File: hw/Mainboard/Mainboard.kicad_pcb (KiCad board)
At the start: 2 copper layers, 262.5 x 95.2 mm, 272 parts, among them J1 SJ-43504-SMT-TR, J10 5V PWR, J11 9V POWER, J12 NOT_HDMI_A, J13 MicroSD, J14 USB2.0_HOST_TYPE_C, J16 MCU, J17 BOOTSEL, J18 PET POWER, J19 PROG, J2 KEYBOARD, J20 5V PWR, J21 FPGA-P4, J22 MENU, J23 FPGA_P2, J24 Conn_02x15_Odd_Even, J3 IEEE, J4 USER, J5 CASS A, J6 CASS B, J7 9V POWER, J8 SPEAKER, J9 VIDEO, Q1 AO3401A, Q2 MMBT3904, Q3 AO3401A, Q4 MMBT3904, SW1 RESET, SW2 RUN, SW3 MENU, SW4 NMI, SW5 CONFIG, U1 74HC154, U10 LM317AG-TN3-R, U11 W65C02S, U12 AS6C1008, U13 AMS1117-3.3, U14 RP2040, U15 LM317AG-TN3-R, U16 W25Q128JVS, U17 LM317AG-TN3-R, U18 SN74LVC4245APWR, U19 SN74LVC4245APWR, U2 SN74LS07, U20 SN74LVC4245APWR, U21 T8Q144C3, U3 SN74LS07, U4 SN74LS07, U5 74LS245, U6 74LS245, U7 W65C21N, U8 W65C21N, U9 W65C22N, Y1 12 MHz

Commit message: wip: support 8x16 keyboard matrix
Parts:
- added C53: 100n, Capacitor_SMD:C_0402_1005Metric, F.Cu at (-113.5, 72.2)
- added J15: KEYBOARDEX, Connector_PinHeader_2.54mm:PinHeader_1x09_P2.54mm_Vertical, F.Cu at (-92.9, 81.3)
- added Q5: SS8550, Package_TO_SOT_SMD:SOT-23, F.Cu at (-100.4, 72.8)
- added R48: 33, Resistor_SMD:R_0402_1005Metric, F.Cu at (-19.7, 56.3)
- added R51: 33, Resistor_SMD:R_0402_1005Metric, F.Cu at (-20.9, 54.3)
- added R63: 33, Resistor_SMD:R_0402_1005Metric, F.Cu at (-15.9, 54.3)
- added R67: 33, Resistor_SMD:R_0402_1005Metric, F.Cu at (-17.1, 54.3)
- added R68: 33, Resistor_SMD:R_0402_1005Metric, F.Cu at (-54.0, 42.2)
- added R69: 33, Resistor_SMD:R_0402_1005Metric, F.Cu at (-4.26, 62.1)
- added R70: 33, Resistor_SMD:R_0402_1005Metric, F.Cu at (-52.0, 32.5)
- added R71: 33, Resistor_SMD:R_0402_1005Metric, F.Cu at (-52.0, 38.1)
- added R72: 2k2, Resistor_SMD:R_0402_1005Metric, F.Cu at (-101.5, 75.0)
- added R73: 2k2, Resistor_SMD:R_0402_1005Metric, F.Cu at (-101.4, 70.5)
- added R74: 2k2, Resistor_SMD:R_0402_1005Metric, F.Cu at (-99.5, 75.0)
- added U22: 74LS145, Package_SO:SOIC-16_3.9x9.9mm_P1.27mm, F.Cu at (-107.7, 74.8)
- J16: footprint Connector_PinHeader_2.54mm:PinHeader_2x10_P2.54mm_Vertical -> Connector_PinHeader_2.54mm:PinHeader_2x12_P2.54mm_Vertical
- U1: value 74HC154 -> 74LS145; footprint Package_SO:TSSOP-24_4.4x7.8mm_P0.65mm -> Package_SO:SOIC-16_3.9x9.9mm_P1.27mm
- moved R66 48.7 mm to (-18.5, 22.3)
- moved C1 9.87 mm to (-126.3, 72.3), turned to -90 degrees
- moved U1 8.93 mm to (-120.5, 74.8)
- moved R21 4.00 mm to (-21.9, 60.6)
- moved R65 3.61 mm to (-37.6, 26.7)
- moved RN10 2.78 mm to (-130.0, 79.2)
- moved J16 2.55 mm to (-47.1, 22.3)
- moved R52 2.54 mm to (-71.2, 7.70)
- moved R54 2.54 mm to (-73.2, 7.70)
- moved R55 2.54 mm to (-71.2, 5.30)
- moved R57 2.54 mm to (-71.2, 6.35)
- moved R58 2.54 mm to (-73.2, 6.35)
- moved R60 2.54 mm to (-73.2, 5.30)
- moved R64 2.31 mm to (-38.6, 25.6)
- moved U20 2.18 mm to (-93.0, 61.3)
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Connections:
- C1 pad 1: Net-(C1-Pad1) -> /Keyboard/VCC
- C1 pad 2: Net-(C1-Pad2) -> /Keyboard/VSS
- J13 pad 3: /MAGIC/MCU/SPI1_TX -> /MAGIC/FPGA/SPI0_TX
- J13 pad 5: /MAGIC/MCU/SPI1_SCK -> /MAGIC/FPGA/SPI0_SCK
- J13 pad 7: /MAGIC/MCU/SPI1_RX -> Net-(J13-Pad7)
- J16 pad 10: /MAGIC/MCU/SPI1_~{READY} -> /MAGIC/FPGA/YY1
- J16 pad 11: /MAGIC/MCU/SPI0_SCK -> /MAGIC/FPGA/YY2
- J16 pad 12: /MAGIC/MCU/SPI1_RX -> /MAGIC/FPGA/YY3
- J16 pad 13: /MAGIC/MCU/SPI0_TX -> /MAGIC/FPGA/YY4
- J16 pad 14: /MAGIC/MCU/SPI1_~{CS} -> /MAGIC/FPGA/SPI1_~{READY}
- J16 pad 15: /MAGIC/MCU/SPI0_RX -> /MAGIC/FPGA/YY5
- J16 pad 16: /MAGIC/MCU/SPI1_SCK -> /MAGIC/FPGA/SPI1_~{CS}
- J16 pad 17: unconnected-(J16-Pad17) -> /MAGIC/MCU/I2C0_SDA
- J16 pad 18: /MAGIC/MCU/SPI1_TX -> /MAGIC/FPGA/SPI1_SCK
- J16 pad 19: unconnected-(J16-Pad19) -> /MAGIC/MCU/I2C0_SCL
- J16 pad 2: +3V3 -> +1V1
- J16 pad 20: GND -> /MAGIC/FPGA/SPI1_TX
- J16 pad 3: /MAGIC/MCU/I2C0_SDA -> /MAGIC/FPGA/SPI0_~{CS}
- J16 pad 4: /MAGIC/MCU/I2C1_SDA -> /MAGIC/FPGA/I2C1_SDA
- J16 pad 5: /MAGIC/MCU/I2C0_SCL -> /MAGIC/FPGA/SPI0_SCK
- J16 pad 6: /MAGIC/MCU/I2C1_SCL -> /MAGIC/FPGA/I2C1_SCL
- J16 pad 7: GND -> /MAGIC/FPGA/SPI0_TX
- J16 pad 8: /MAGIC/MCU/CEC -> /MAGIC/FPGA/YY6
- J16 pad 9: /MAGIC/MCU/SPI0_~{CS} -> /MAGIC/FPGA/SPI0_RX
- J19 pad 12: /MAGIC/MCU/SPI0_~{CS} -> /MAGIC/FPGA/SPI0_~{CS}
- J21 pad 11: /MAGIC/FPGA/R76 -> /MAGIC/FPGA/L75
- J21 pad 12: GND -> /MAGIC/FPGA/R76
- J21 pad 15: /MAGIC/FPGA/FPGA_CLK -> /MAGIC/FPGA/S1
- J21 pad 16: unconnected-(J21-Pad16) -> /MAGIC/FPGA/FPGA_CLK
- J21 pad 17: /MAGIC/FPGA/S2 -> /MAGIC/FPGA/NSTATUS
- J21 pad 18: /MAGIC/FPGA/S1 -> /MAGIC/FPGA/S2
- J21 pad 19: /MAGIC/FPGA/S3 -> /MAGIC/FPGA/S4
- J21 pad 20: /MAGIC/FPGA/NSTATUS -> /MAGIC/FPGA/S3
- J21 pad 21: /MAGIC/FPGA/L68 -> /MAGIC/FPGA/L67
- J21 pad 22: /MAGIC/FPGA/S4 -> /CPU \ RAM/~{NMI}
- J21 pad 23: /MAGIC/FPGA/L65 -> /MAGIC/FPGA/L66
- J21 pad 24: /MAGIC/FPGA/L67 -> /MAGIC/FPGA/L65
- J21 pad 25: /MAGIC/FPGA/L64 -> /MAGIC/FPGA/L53
- J21 pad 26: /MAGIC/FPGA/L66 -> /MAGIC/FPGA/L64
- J23 pad 10: /MAGIC/FPGA/N02 -> /MAGIC/FPGA/N04
- J23 pad 11: unconnected-(J23-Pad11) -> /MAGIC/FPGA/P06
- J23 pad 12: unconnected-(J23-Pad12) -> /MAGIC/FPGA/N06
- J23 pad 13: /MAGIC/FPGA/DIAG -> /MAGIC/FPGA/P09
- J23 pad 14: /MAGIC/FPGA/VIA_CB2 -> /MAGIC/FPGA/N09
- J23 pad 15: /MAGIC/FPGA/GRAPHICS -> /MAGIC/FPGA/DIAG
- J23 pad 16: /MAGIC/FPGA/~{RAM_OE} -> /MAGIC/FPGA/VIA_CB2
- J23 pad 17: /MAGIC/FPGA/~{RAM_WE} -> /MAGIC/FPGA/GRAPHICS
- J23 pad 18: /MAGIC/FPGA/~{VP} -> /MAGIC/FPGA/~{RAM_OE}
- J23 pad 19: /MAGIC/FPGA/RDY -> /MAGIC/FPGA/~{RAM_WE}
- J23 pad 20: /CPU \ RAM/~{RES} -> /MAGIC/FPGA/~{VP}
- J23 pad 21: /MAGIC/FPGA/~{SO} -> /MAGIC/FPGA/RDY
- J23 pad 22: /MAGIC/FPGA/~{IRQ} -> /MAGIC/FPGA/~{SO}
- J23 pad 23: /MAGIC/FPGA/~{ML} -> /MAGIC/FPGA/~{IRQ}
- J23 pad 24: /MAGIC/FPGA/BE -> /MAGIC/FPGA/~{ML}
- J23 pad 25: /CPU \ RAM/~{NMI} -> /MAGIC/FPGA/BE
- J23 pad 27: GND -> /CPU \ RAM/~{RES}
- J23 pad 3: GND -> unconnected-(J23-Pad3)
- J23 pad 4: /MAGIC/FPGA/AUDIO -> unconnected-(J23-Pad4)
- J23 pad 5: unconnected-(J23-Pad5) -> /MAGIC/FPGA/AUDIO
- J23 pad 7: unconnected-(J23-Pad7) -> /MAGIC/FPGA/P02
- J23 pad 8: /MAGIC/FPGA/P02 -> /MAGIC/FPGA/N02
- J23 pad 9: unconnected-(J23-Pad9) -> /MAGIC/FPGA/P04
- JP7 pad 1: /MAGIC/MCU/CEC -> /MAGIC/FPGA/CEC
- PT17 pad 2: Net-(C1-Pad1) -> /Keyboard/VCC
- PT33 pad 2: Net-(C1-Pad2) -> /Keyboard/VSS
- R19 pad 1: /MAGIC/MCU/SPI0_SCK -> /MAGIC/FPGA/SPI0_SCK
- R22 pad 1: /MAGIC/MCU/SPI1_SCK -> /MAGIC/FPGA/SPI1_SCK
- R64 pad 2: /MAGIC/MCU/I2C1_SDA -> /MAGIC/FPGA/I2C1_SDA
- R65 pad 2: /MAGIC/MCU/I2C1_SCL -> /MAGIC/FPGA/I2C1_SCL
- RN10 pad 5: Net-(C1-Pad1) -> /Keyboard/VCC
- RN10 pad 6: Net-(C1-Pad1) -> /Keyboard/VCC
- RN10 pad 7: Net-(C1-Pad1) -> /Keyboard/VCC
- RN10 pad 8: Net-(C1-Pad1) -> /Keyboard/VCC
- RN16 pad 3: /MAGIC/MCU/SPI1_TX -> /MAGIC/FPGA/SPI0_TX
- RN16 pad 4: /MAGIC/MCU/SPI1_RX -> /MAGIC/FPGA/SPI0_RX
- RN9 pad 5: Net-(C1-Pad1) -> /Keyboard/VCC
- RN9 pad 6: Net-(C1-Pad1) -> /Keyboard/VCC
- RN9 pad 7: Net-(C1-Pad1) -> /Keyboard/VCC
- RN9 pad 8: Net-(C1-Pad1) -> /Keyboard/VCC
- U1 pad 10: /Keyboard/R9 -> /Keyboard/R8
- U1 pad 11: unconnected-(U1-Pad11) -> /Keyboard/R9
- U1 pad 12: Net-(C1-Pad2) -> /IO/KEY_ROW3
- U1 pad 13: unconnected-(U1-Pad13) -> /IO/KEY_ROW2
- U1 pad 14: unconnected-(U1-Pad14) -> /IO/KEY_ROW1
- U1 pad 15: unconnected-(U1-Pad15) -> /IO/KEY_ROW0
- U1 pad 16: unconnected-(U1-Pad16) -> /Keyboard/VCC
- U1 pad 8: /Keyboard/R7 -> /Keyboard/VSS
- U1 pad 9: /Keyboard/R8 -> /Keyboard/R7
- U14 pad 13: /MAGIC/MCU/SPI1_~{READY} -> /MAGIC/FPGA/SPI1_~{READY}
- U14 pad 14: /MAGIC/MCU/MCU_FPGA_CLK -> /MAGIC/MCU/MCU_SPI1_TX
- U14 pad 15: /MAGIC/MCU/SPI1_RX -> /MAGIC/FPGA/SPI1_RX
- U14 pad 16: /MAGIC/MCU/SPI1_~{CS} -> /MAGIC/MCU/MCU_SPI1_~{CS}
- U14 pad 18: /MAGIC/MCU/SPI1_TX -> /MAGIC/MCU/MCU_FPGA_CLK
- U14 pad 36: /MAGIC/MCU/CEC -> /MAGIC/FPGA/CEC
- U14 pad 4: /MAGIC/MCU/I2C1_SDA -> /MAGIC/FPGA/I2C1_SDA
- U14 pad 5: /MAGIC/MCU/I2C1_SCL -> /MAGIC/FPGA/I2C1_SCL
- U14 pad 6: /MAGIC/MCU/SPI0_RX -> /MAGIC/FPGA/SPI0_RX
- U14 pad 7: /MAGIC/MCU/SPI0_~{CS} -> /MAGIC/MCU/MCU_SPI0_~{CS}
- U14 pad 9: /MAGIC/MCU/SPI0_TX -> /MAGIC/MCU/MCU_SPI0_TX
- U21 pad 10: /MAGIC/MCU/SPI1_~{CS} -> /MAGIC/FPGA/SPI1_~{CS}
- U21 pad 11: /MAGIC/MCU/SPI1_SCK -> /MAGIC/FPGA/SPI1_SCK
- U21 pad 119: /MAGIC/~{PIA2_CS} -> /MAGIC/~{IO_OE}
- U21 pad 123: /MAGIC/~{IO_OE} -> /MAGIC/~{PIA2_CS}
- U21 pad 131: unconnected-(U21-Pad131) -> /MAGIC/FPGA/L75
- U21 pad 139: /MAGIC/FPGA/L68 -> /CPU \ RAM/~{NMI}
- U21 pad 14: /MAGIC/MCU/I2C1_SCL -> /MAGIC/FPGA/FPGA_SPI1_~{READY}
- U21 pad 15: /MAGIC/MCU/I2C1_SDA -> /MAGIC/FPGA/I2C1_SCL
- U21 pad 16: unconnected-(U21-Pad16) -> /MAGIC/FPGA/I2C1_SDA
- U21 pad 17: unconnected-(U21-Pad17) -> /MAGIC/FPGA/YY4
- U21 pad 18: /MAGIC/MCU/SPI1_~{READY} -> /MAGIC/FPGA/YY3
- U21 pad 19: unconnected-(U21-Pad19) -> /MAGIC/FPGA/YY2
- U21 pad 20: unconnected-(U21-Pad20) -> /MAGIC/FPGA/YY1
- U21 pad 28: /MAGIC/MCU/SPI0_RX -> /MAGIC/FPGA/FPGA_SPI0_TX
- U21 pad 29: /MAGIC/MCU/SPI0_TX -> /MAGIC/FPGA/SPI0_TX
- U21 pad 3: unconnected-(U21-Pad3) -> /MAGIC/FPGA/L53
- U21 pad 30: /MAGIC/MCU/SPI0_SCK -> /MAGIC/FPGA/SPI0_SCK
- U21 pad 31: /MAGIC/MCU/SPI0_~{CS} -> /MAGIC/FPGA/SPI0_~{CS}
- U21 pad 33: /MAGIC/MCU/CEC -> /MAGIC/FPGA/YY6
- U21 pad 4: unconnected-(U21-Pad4) -> /MAGIC/FPGA/CEC
- U21 pad 42: unconnected-(U21-Pad42) -> /MAGIC/FPGA/P04
- U21 pad 43: unconnected-(U21-Pad43) -> /MAGIC/FPGA/N04
- U21 pad 45: unconnected-(U21-Pad45) -> /MAGIC/FPGA/P06
- U21 pad 46: unconnected-(U21-Pad46) -> /MAGIC/FPGA/N06
- U21 pad 47: unconnected-(U21-Pad47) -> /MAGIC/FPGA/P09
- U21 pad 48: /MAGIC/FPGA/DIAG -> /MAGIC/FPGA/N09
- U21 pad 53: /MAGIC/FPGA/VIA_CB2 -> /MAGIC/FPGA/DIAG
- U21 pad 54: /MAGIC/FPGA/GRAPHICS -> /MAGIC/FPGA/VIA_CB2
- U21 pad 55: /MAGIC/FPGA/~{RAM_OE} -> /MAGIC/FPGA/GRAPHICS
- U21 pad 56: /MAGIC/FPGA/~{RAM_WE} -> /MAGIC/FPGA/~{RAM_OE}
- U21 pad 58: /MAGIC/FPGA/~{VP} -> /MAGIC/FPGA/~{RAM_WE}
- U21 pad 59: /MAGIC/FPGA/RDY -> /MAGIC/FPGA/~{VP}
- U21 pad 6: unconnected-(U21-Pad6) -> /MAGIC/FPGA/YY5
- U21 pad 60: /MAGIC/FPGA/~{SO} -> /MAGIC/FPGA/RDY
- U21 pad 61: /MAGIC/FPGA/~{IRQ} -> /MAGIC/FPGA/~{SO}
- U21 pad 65: /MAGIC/FPGA/~{ML} -> /MAGIC/FPGA/~{IRQ}
- U21 pad 66: /MAGIC/FPGA/BE -> /MAGIC/FPGA/~{ML}
- U21 pad 67: /CPU \ RAM/~{NMI} -> /MAGIC/FPGA/BE
- U21 pad 7: /MAGIC/MCU/SPI1_TX -> /MAGIC/FPGA/FPGA_SPI1_TX
- U21 pad 8: /MAGIC/MCU/SPI1_RX -> /MAGIC/FPGA/SPI1_TX
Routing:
- net /MAGIC/MCU/SPI0_~{CS}: track 105.9 -> 0.00 mm, vias 1 -> 0
- net /Keyboard/VCC: track 0.00 -> 90.7 mm
- net /MAGIC/FPGA/SPI0_~{CS}: track 0.00 -> 88.3 mm, vias 0 -> 1
- net /MAGIC/MCU/SPI1_TX: track 88.1 -> 0.00 mm, vias 3 -> 0
- net /MAGIC/MCU/I2C1_SDA: track 84.5 -> 0.00 mm, vias 2 -> 0
- net /MAGIC/FPGA/SPI0_TX: track 0.00 -> 83.9 mm, vias 0 -> 2
- net /MAGIC/MCU/SPI1_RX: track 79.3 -> 0.00 mm, vias 4 -> 0
- net /MAGIC/FPGA/SPI0_RX: track 0.00 -> 79.0 mm, vias 0 -> 4
- net /MAGIC/FPGA/I2C1_SDA: track 0.00 -> 78.5 mm, vias 0 -> 1
- net /MAGIC/FPGA/SPI0_SCK: track 0.00 -> 74.4 mm, vias 0 -> 2
- net /MAGIC/FPGA/I2C1_SCL: track 0.00 -> 71.1 mm
- net /MAGIC/MCU/SPI1_SCK: track 70.3 -> 0.00 mm, vias 3 -> 0
- net Net-(D6-Pad1): track 264.8 -> 195.4 mm
- net /MAGIC/MCU/CEC: track 68.8 -> 0.00 mm, vias 1 -> 0
- net /MAGIC/MCU/I2C1_SCL: track 68.5 -> 0.00 mm, vias 2 -> 0
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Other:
- board text added: "R12"
- board text added: "R13"
- board text added: "R14"
- board text removed: "50M"

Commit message: wip: keyboard ex header
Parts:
- removed C53: 100n, Capacitor_SMD:C_0402_1005Metric
- removed Q5: SS8550, Package_TO_SOT_SMD:SOT-23
- removed R72, R73, R74: 2k2, Resistor_SMD:R_0402_1005Metric
- removed U22: 74LS145, Package_SO:SOIC-16_3.9x9.9mm_P1.27mm
- J15: value KEYBOARDEX -> KEYBOARD_EX; footprint Connector_PinHeader_2.54mm:PinHeader_1x09_P2.54mm_Vertical -> Connector_PinHeader_2.54mm:PinHeader_2x08_P2.54mm_Vertical
- PT33: moved to B.Cu
- moved J15 32.1 mm to (-123.4, 71.1)
- moved U1 9.96 mm to (-110.9, 77.5)
- moved C1 9.88 mm to (-116.8, 75.0)
- moved PT17 1.19 mm to (-143.9, 77.1)
- moved RN10 0.38 mm to (-130.0, 78.8)
- moved RN9 0.38 mm to (-136.1, 78.8)
- moved C8 0.10 mm to (-190.3, 59.6), turned to -90 degrees
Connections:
- J15 pad 2: /CPU \ RAM/~{NMI} -> /IO/KEY_COL7
- J15 pad 3: /Keyboard/VCC -> /CPU \ RAM/~{NMI}
- J15 pad 4: /Keyboard/R15 -> /IO/KEY_COL6
- J15 pad 5: /Keyboard/R14 -> /Keyboard/VCC
- J15 pad 6: /Keyboard/R13 -> /IO/KEY_COL5
- J15 pad 7: /Keyboard/R12 -> /Keyboard/VSS
- J15 pad 8: /Keyboard/R11 -> /IO/KEY_COL4
- J15 pad 9: /Keyboard/R10 -> /IO/KEY_ROW3
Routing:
- net /IO/KEY_ROW3: track 149.6 -> 104.7 mm, vias 3 -> 1
- net /CPU \ RAM/~{RES}: track 172.0 -> 213.7 mm, vias 3 -> 2
- net +3V3: track 541.2 -> 501.8 mm
- net /Keyboard/VCC: track 90.7 -> 55.8 mm
- net /IO/KEY_COL6: track 58.6 -> 82.8 mm, vias 1 -> 0
- net /IO/KEY_COL4: track 65.3 -> 84.9 mm, vias 0 -> 1
- net /IO/KEY_COL3: track 61.1 -> 79.1 mm
- net /IO/KEY_COL5: track 63.1 -> 80.3 mm, vias 1 -> 0
- net /CASS/CASS_WRITE: track 269.2 -> 254.7 mm, vias 6 -> 5
- net Net-(U22-Pad12): track 13.8 -> 0.00 mm
- net /CPU \ RAM/~{NMI}: track 189.6 -> 175.9 mm
- net /Keyboard/R9: track 31.4 -> 18.5 mm, vias 1 -> 0
- net /IEEE/SRQ: track 224.0 -> 212.5 mm
- net GND: track 1363.5 -> 1352.5 mm, vias 48 -> 46
- net /Keyboard/R6: track 15.8 -> 4.89 mm, vias 1 -> 0
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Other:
- board text added: "K0"
- board text added: "K1"
- board text added: "K2"
- board text added: "K3"
- board text removed: "R12"
- board text removed: "R13"
- board text removed: "R14"

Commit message: hw: autoroute
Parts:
- removed Q2: MMBT3904, Package_TO_SOT_SMD:SOT-23
- removed RV1: 20k, Potentiometer_SMD:Potentiometer_Bourns_TC33X_Vertical
- added J25: IEEE_HEADER, Connector_PinHeader_2.54mm:PinHeader_2x09_P2.54mm_Vertical, F.Cu at (-187.5, -0.70)
- added J26: USER_HEADER, Connector_PinHeader_2.54mm:PinHeader_2x11_P2.54mm_Vertical, F.Cu at (-104.9, -0.70)
- added J27: CASS_A_HEADER, Connector_PinHeader_2.54mm:PinHeader_1x06_P2.54mm_Vertical, F.Cu at (-12.1, -3.25)
- added J28: CASS_B_HEADER, Connector_PinHeader_2.54mm:PinHeader_1x06_P2.54mm_Vertical, F.Cu at (-177.1, 73.2)
- added R72: 22k, Resistor_SMD:R_0402_1005Metric, F.Cu at (-4.38, 35.0)
- added U22: 74HC04, Package_SO:SOIC-14_3.9x8.7mm_P1.27mm, F.Cu at (-4.00, 30.0)
- J8: value SPEAKER -> LINE_AUDIO; footprint PET:PET_SPEAKER -> Connector_PinHeader_2.54mm:PinHeader_1x02_P2.54mm_Vertical
- LS1: footprint SnapEDA:XDCR_AT-1224-TWT-5V-2-R -> SamacSys_Parts:AT1220TT9R
- R53: value 22k -> 4k7
- R61: value 4k7 -> 220; footprint Resistor_SMD:R_0402_1005Metric -> Resistor_SMD:R_0603_1608Metric
- R62: value 330 -> 220; footprint Resistor_SMD:R_0805_2012Metric -> Resistor_SMD:R_0603_1608Metric
- moved PT26 75.8 mm to (-74.6, -1.15), turned to 180 degrees
- moved LS1 28.2 mm to (1.22, 17.7), turned to -90 degrees
- moved PT17 24.2 mm to (-122.1, 87.6), turned to 90 degrees
- moved J8 15.4 mm to (3.35, 32.0), turned to 0 degrees
- moved C30 13.9 mm to (-11.9, 38.9), turned to -90 degrees
- moved C31 11.0 mm to (-6.35, 35.0), turned to 0 degrees
- moved Q1 8.85 mm to (-188.3, 70.9)
- moved J17 8.78 mm to (-11.1, 48.3), turned to 180 degrees
- moved R53 7.86 mm to (-8.32, 34.3), turned to 0 degrees
- moved PT22 7.57 mm to (-189.6, 68.2), turned to 0 degrees
- moved R50 7.10 mm to (-2.62, -0.83), turned to -90 degrees
- moved JP1 6.91 mm to (-178.4, 59.4)
- moved JP4 6.89 mm to (-183.5, 62.3)
- moved JP5 6.89 mm to (-178.4, 65.2)
- moved JP6 6.89 mm to (-183.5, 65.2)
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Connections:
- C30 pad 1: Net-(C30-Pad1) -> +3V3
- J1 pad 2: Net-(C31-Pad2) -> Net-(J1-Pad2)
- J1 pad 3: Net-(C31-Pad2) -> Net-(J1-Pad2)
- J1 pad 4: unconnected-(J1-Pad4) -> Net-(J1-Pad4)
- J19 pad 10: unconnected-(J19-Pad10) -> +5V
- LS1 pad 1: Net-(J8-Pad4) -> Net-(LS1-Pad1)
- LS1 pad 2: GND -> Net-(LS1-Pad2)
- PT26 pad 1: +6V -> +5V
- PT26 pad 2: Net-(C30-Pad1) -> /USER/VCC
- R53 pad 1: Net-(C30-Pad1) -> /MAGIC/FPGA/AUDIO
- R53 pad 2: Net-(Q2-Pad1) -> Net-(J1-Pad4)
- R61 pad 1: Net-(Q2-Pad1) -> Net-(LS1-Pad1)
- R61 pad 2: GND -> Net-(R61-Pad2)
- R62 pad 1: Net-(J8-Pad4) -> Net-(LS1-Pad2)
- R62 pad 2: GND -> Net-(R62-Pad2)
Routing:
- net GND: track 1352.5 -> 1251.2 mm, vias 46 -> 60
- net +6V: track 306.8 -> 258.6 mm, vias 6 -> 2
- net /USER/VCC: track 0.00 -> 43.7 mm, vias 0 -> 1
- net /IEEE/IFC_OUT: track 85.1 -> 124.9 mm
- net /CASS/CASS2_READ: track 165.5 -> 203.8 mm, vias 3 -> 8
- net /CASS/~{CASS1_SWITCH}: track 96.2 -> 62.5 mm
- net /IEEE/DIO6: track 116.5 -> 149.1 mm
- net Net-(J8-Pad4): track 32.0 -> 0.00 mm
- net Net-(J1-Pad2): track 0.00 -> 29.7 mm, vias 0 -> 2
- net Net-(C31-Pad2): track 30.5 -> 0.99 mm
- net /IEEE/ATN_OUT: track 65.6 -> 91.9 mm
- net Net-(J1-Pad4): track 0.00 -> 26.0 mm
- net /IO/VIA_PA4: track 112.3 -> 137.0 mm, vias 2 -> 4
- net /IO/VIA_PA6: track 105.0 -> 129.2 mm
- net /MAGIC/FPGA/SPI0_SCK: track 75.4 -> 99.6 mm
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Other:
- board text removed: "MCU"
- board text removed: "SP+"
- board text removed: "SP-"
- board text removed: "SPEAKER"

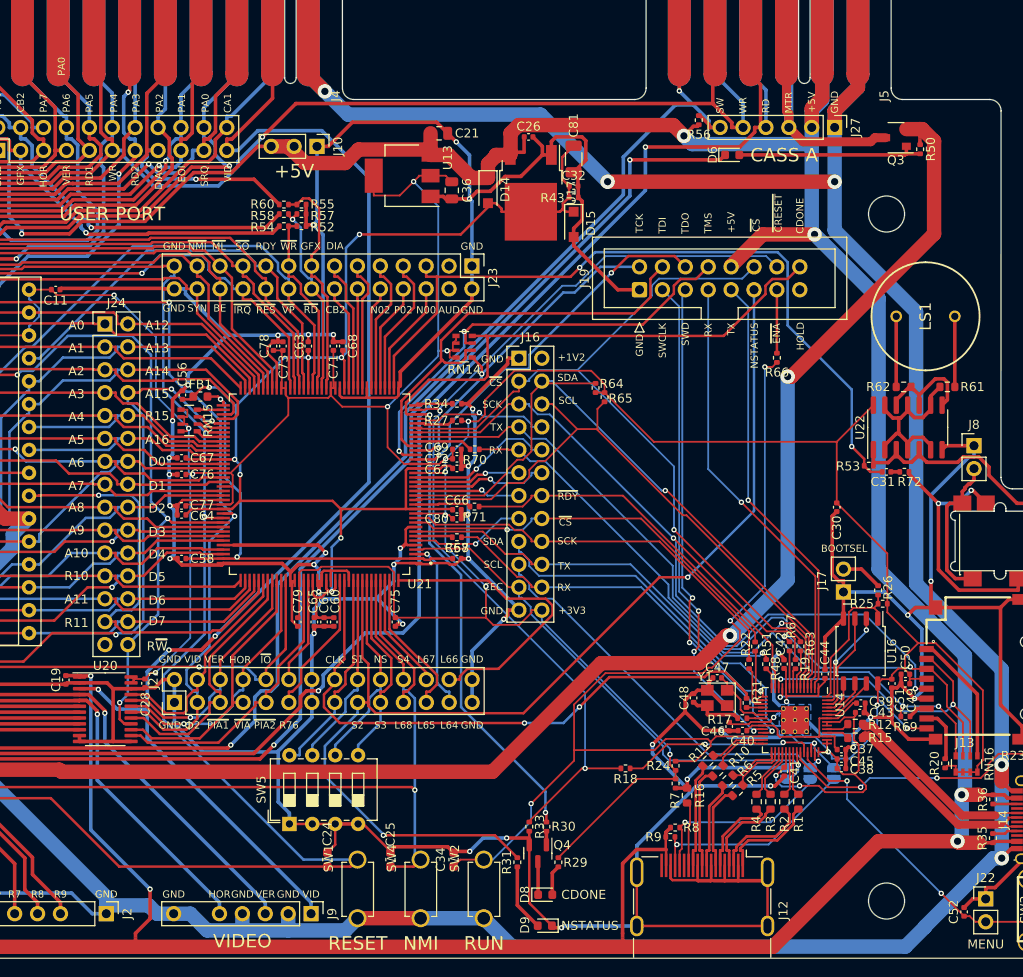
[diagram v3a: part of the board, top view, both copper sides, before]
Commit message: hw: update 10u caps
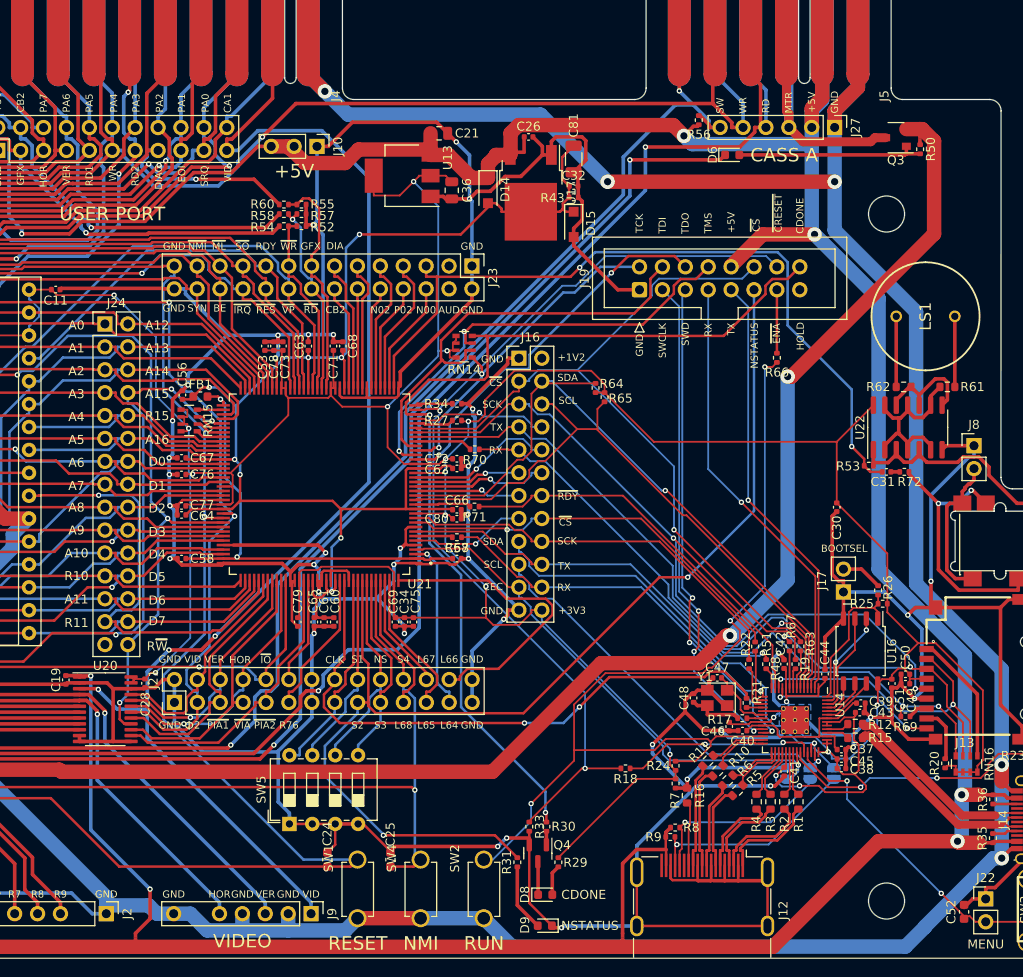
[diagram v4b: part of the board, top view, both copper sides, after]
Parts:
- added C53: 1u, Capacitor_SMD:C_0402_1005Metric, F.Cu at (-75.3, 21.0)
- C13, C22, C26: value 100n -> 100n 50V
- C34: value 10u -> 100n; footprint Capacitor_SMD:C_0603_1608Metric -> Capacitor_SMD:C_0402_1005Metric
- C52: value 1u -> 10u; footprint Capacitor_SMD:C_0402_1005Metric -> Capacitor_SMD:C_0603_1608Metric
- C69: value 1u -> 10n
- C73: value 100n -> 10n
- C75: value 100n -> 1u
- C78, C79: value 10n -> 100n
- moved C34 26.9 mm to (-59.8, 51.6), turned to -90 degrees
- moved C69 20.3 mm to (-60.8, 51.6), turned to -90 degrees
- moved C75 2.00 mm to (-58.8, 51.6)
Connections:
- C34 pad 1: /MAGIC/MCU/RUN -> +3V3
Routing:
- net /MAGIC/MCU/RUN: track 107.7 -> 104.0 mm
- net GND: track 1251.2 -> 1253.8 mm, vias 60 -> 61
- net /CASS/CASS_A_READ: track 220.0 -> 220.7 mm

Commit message: hw: wip
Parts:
- removed J17: BOOTSEL, Connector_PinHeader_2.54mm:PinHeader_1x02_P2.54mm_Vertical
- added C54: 47u 10V, Capacitor_SMD:C_1206_3216Metric, F.Cu at (4.82, 27.2)
- added C55: 47n, Capacitor_SMD:C_0402_1005Metric, F.Cu at (4.82, 30.1)
- added C59: 22n, Capacitor_SMD:C_0402_1005Metric, F.Cu at (-6.33, 38.4)
- added C70: 10u, Capacitor_SMD:C_0603_1608Metric, F.Cu at (-36.4, 65.0)
- added C74: 100n, Capacitor_SMD:C_0402_1005Metric, F.Cu at (-47.0, 74.3)
- added PT34: PowerTie_2, PET:NetTie-2_SMD_Pad_1.6_to_0.4mm, F.Cu at (-240.1, 37.9)
- added PT35: PowerTie_2, PET:NetTie-2_SMD_Pad_1.6_to_0.4mm, F.Cu at (-0.75, 27.2)
- added PT36: PowerTie_2, PET:NetTie-2_SMD_Pad_1.6_to_0.4mm, F.Cu at (1.27, 23.9)
- added PT38: PowerTie_2, PET:NetTie-2_SMD_Pad_1.6_to_0.4mm, F.Cu at (-3.29, 38.4)
- added R73: 5k1, Resistor_SMD:R_0402_1005Metric, F.Cu at (3.95, 72.0)
- added R74: 5k1, Resistor_SMD:R_0402_1005Metric, F.Cu at (3.95, 75.1)
- C35: footprint PET:CP_Radial_D16.0mm_P5.00mm_P7.50mm -> PET:CP_Radial_D18.0mm_P5.00mm_P7.50mm
- C62, C63: value 100n -> 10n
- C66, C68: value 10n -> 100n
- J10, J20: footprint Connector_PinHeader_2.54mm:PinHeader_1x03_P2.54mm_Vertical -> Connector_PinHeader_2.54mm:PinHeader_2x03_P2.54mm_Vertical
- J8: value LINE_AUDIO -> BOOTSEL; footprint Connector_PinHeader_2.54mm:PinHeader_1x02_P2.54mm_Vertical -> Connector_PinHeader_2.54mm:PinHeader_1x04_P2.54mm_Vertical
- JP1, JP2, JP3, JP4, JP5, JP6: footprint Jumper:SolderJumper-3_P1.3mm_Bridged12_RoundedPad1.0x1.5mm -> Jumper:SolderJumper-3_P1.3mm_Open_RoundedPad1.0x1.5mm
- R24: value 10k -> 15k
- R53: footprint Resistor_SMD:R_0402_1005Metric -> Resistor_SMD:R_0805_2012Metric_Pad1.20x1.40mm_HandSolder
- R61: value 220 -> 10; footprint Resistor_SMD:R_0603_1608Metric -> Resistor_SMD:R_0805_2012Metric_Pad1.20x1.40mm_HandSolder
- R62: value 220 -> 33; footprint Resistor_SMD:R_0603_1608Metric -> Resistor_SMD:R_0402_1005Metric
- R72: value 22k -> 12k; footprint Resistor_SMD:R_0402_1005Metric -> Resistor_SMD:R_0805_2012Metric_Pad1.20x1.40mm_HandSolder
- SW3: footprint JLCPCB:KEY-TH_SKHLLBA010 -> PET:APEM_MJTP1117
- U22: value 74HC04 -> LM386; footprint Package_SO:SOIC-14_3.9x8.7mm_P1.27mm -> Package_DIP:DIP-8_W7.62mm
- moved R62 49.6 mm to (-54.0, 28.4)
- moved R66 49.0 mm to (-40.1, 66.3), turned to 90 degrees
- moved J8 45.6 mm to (-11.3, 75.2), turned to 90 degrees
- moved C81 24.3 mm to (-64.9, 4.85), turned to 180 degrees
- moved C21 18.5 mm to (-39.4, 5.45), turned to -90 degrees
- moved C30 18.4 mm to (0.79, 25.5), turned to 0 degrees
- moved U13 15.6 mm to (-44.9, 5.45)
- moved D14 13.5 mm to (-63.8, 1.40)
- moved C26 13.4 mm to (-59.5, -2.45)
- moved U17 13.2 mm to (-59.0, 3.65)
- moved R43 13.1 mm to (-53.8, 1.75)
- moved C32 12.8 mm to (-53.9, 2.80)
- moved D15 12.5 mm to (-53.2, 4.55), turned to 0 degrees
- moved PT14 12.4 mm to (-60.0, -4.05), turned to -90 degrees
- moved C36 11.6 mm to (-44.9, 10.1), turned to 0 degrees
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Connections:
- net /MAGIC/FPGA/YY5 renamed /MAGIC/FPGA/L46
- C30 pad 1: +3V3 -> Net-(C30-Pad1)
- C30 pad 2: GND -> Net-(C30-Pad2)
- D9 pad 1: GND -> /MAGIC/FPGA/NSTATUS
- J1 pad 4: Net-(J1-Pad4) -> unconnected-(J1-Pad4)
- J10 pad 1: GND -> PD_GND
- J10 pad 3: +5V -> PD_GND
- J16 pad 10: /MAGIC/FPGA/YY1 -> /MAGIC/FPGA/L20
- J16 pad 11: /MAGIC/FPGA/YY2 -> /MAGIC/FPGA/I2C1_SDA
- J16 pad 12: /MAGIC/FPGA/YY3 -> /MAGIC/FPGA/L21
- J16 pad 13: /MAGIC/FPGA/YY4 -> /MAGIC/FPGA/I2C1_SCL
- J16 pad 2: +1V1 -> GND
- J16 pad 23: GND -> +3V3
- J16 pad 4: /MAGIC/FPGA/I2C1_SDA -> /MAGIC/FPGA/AUDIO
- J16 pad 6: /MAGIC/FPGA/I2C1_SCL -> /MAGIC/FPGA/L12
- J16 pad 8: /MAGIC/FPGA/YY6 -> /MAGIC/FPGA/L13
- J20 pad 1: GND -> PD_GND
- J20 pad 3: +5V -> PD_GND
- J21 pad 19: /MAGIC/FPGA/S4 -> /MAGIC/FPGA/CBSEL1
- J21 pad 20: /MAGIC/FPGA/S3 -> /MAGIC/FPGA/CBSEL0
- J21 pad 21: /MAGIC/FPGA/L67 -> /MAGIC/FPGA/S4
- J21 pad 22: /CPU \ RAM/~{NMI} -> /MAGIC/FPGA/S3
- J21 pad 24: /MAGIC/FPGA/L65 -> /CPU \ RAM/~{NMI}
- J23 pad 1: GND -> +3V3
- J23 pad 10: /MAGIC/FPGA/N04 -> /MAGIC/FPGA/N06
- J23 pad 11: /MAGIC/FPGA/P06 -> /MAGIC/FPGA/P09
- J23 pad 12: /MAGIC/FPGA/N06 -> /MAGIC/FPGA/N09
- J23 pad 13: /MAGIC/FPGA/P09 -> +1V2
- J23 pad 14: /MAGIC/FPGA/N09 -> +1V2
- J23 pad 2: GND -> +3V3
- J23 pad 3: unconnected-(J23-Pad3) -> /MAGIC/FPGA/P00
- J23 pad 4: unconnected-(J23-Pad4) -> /MAGIC/FPGA/N00
- J23 pad 5: /MAGIC/FPGA/AUDIO -> /MAGIC/FPGA/P02
- J23 pad 6: /MAGIC/FPGA/N00 -> /MAGIC/FPGA/N02
- J23 pad 7: /MAGIC/FPGA/P02 -> /MAGIC/FPGA/P04
- J23 pad 8: /MAGIC/FPGA/N02 -> /MAGIC/FPGA/N04
- J23 pad 9: /MAGIC/FPGA/P04 -> /MAGIC/FPGA/P06
- J24 pad 29: unconnected-(J24-Pad29) -> GND
- J8 pad 2: Net-(J1-Pad5) -> /MAGIC/MCU/BOOTSEL
- LS1 pad 1: Net-(LS1-Pad1) -> Net-(C54-Pad2)
- LS1 pad 2: Net-(LS1-Pad2) -> PD_GND
- PT19 pad 1: +5V -> Net-(J8-Pad3)
- PT20 pad 1: +5V -> Net-(J8-Pad3)
- R24 pad 2: /MAGIC/MCU/RUN -> /MAGIC/FPGA/~{SPI_ENA}
- R26 pad 1: /MAGIC/MCU/Flash/BOOTSEL -> /MAGIC/MCU/BOOTSEL
- R28 pad 1: Net-(C14-Pad1) -> Net-(PT34-Pad2)
- R31 pad 2: /MAGIC/FPGA/NSTATUS -> +3V3
- R53 pad 1: /MAGIC/FPGA/AUDIO -> Net-(J1-Pad5)
- R53 pad 2: Net-(J1-Pad4) -> PD_GND
- R61 pad 1: Net-(LS1-Pad1) -> Net-(C55-Pad2)
- R61 pad 2: Net-(R61-Pad2) -> PD_GND
- R62 pad 1: Net-(LS1-Pad2) -> /MAGIC/FPGA/CSO
- R62 pad 2: Net-(R62-Pad2) -> /MAGIC/FPGA/AUDIO
- R66 pad 1: /MAGIC/FPGA/~{SPI_ENA} -> Net-(R66-Pad1)
- R66 pad 2: /MAGIC/MCU/RUN -> /MAGIC/FPGA/~{SPI_ENA}
- SW2 pad 2: /MAGIC/MCU/RUN -> Net-(R66-Pad1)
- SW3 pad 1: /MAGIC/MCU/GP27 -> GND
- SW3 pad 2: GND -> /MAGIC/MCU/GP27
- U14 pad 26: /MAGIC/MCU/RUN -> /MAGIC/FPGA/~{SPI_ENA}
- U21 pad 137: /MAGIC/FPGA/S3 -> /MAGIC/FPGA/CBSEL0
- U21 pad 138: /MAGIC/FPGA/S4 -> /MAGIC/FPGA/CBSEL1
- U21 pad 139: /CPU \ RAM/~{NMI} -> /MAGIC/FPGA/S3
- U21 pad 140: /MAGIC/FPGA/L67 -> /MAGIC/FPGA/S4
- U21 pad 141: /MAGIC/FPGA/L65 -> /CPU \ RAM/~{NMI}
- U21 pad 17: /MAGIC/FPGA/YY4 -> /MAGIC/FPGA/L21
- U21 pad 18: /MAGIC/FPGA/YY3 -> /MAGIC/FPGA/L20
- U21 pad 19: /MAGIC/FPGA/YY2 -> /MAGIC/FPGA/L13
- U21 pad 20: /MAGIC/FPGA/YY1 -> /MAGIC/FPGA/L12
- U21 pad 33: /MAGIC/FPGA/YY6 -> /MAGIC/FPGA/CSO
- U21 pad 38: /MAGIC/FPGA/AUDIO -> /MAGIC/FPGA/P00
- U22 pad 1: Net-(J1-Pad4) -> unconnected-(U22-Pad1)
- U22 pad 2: Net-(R61-Pad2) -> PD_GND
- U22 pad 3: Net-(J1-Pad4) -> Net-(J1-Pad5)
- U22 pad 4: Net-(R61-Pad2) -> PD_GND
- U22 pad 5: Net-(J1-Pad4) -> Net-(C54-Pad1)
- U22 pad 6: Net-(R61-Pad2) -> +6V
- U22 pad 7: GND -> unconnected-(U22-Pad7)
- U22 pad 8: Net-(R62-Pad2) -> unconnected-(U22-Pad8)
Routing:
- net /MAGIC/MCU/RUN: track 104.0 -> 0.00 mm, vias 3 -> 0
- net /MAGIC/FPGA/~{SPI_ENA}: track 7.04 -> 98.5 mm, vias 0 -> 3
- net GND: track 1253.8 -> 1203.2 mm, vias 61 -> 62
- net /MAGIC/MCU/BOOTSEL: track 0.00 -> 46.6 mm, vias 0 -> 3
- net PD_GND: track 808.5 -> 847.9 mm, vias 10 -> 9
- net /MAGIC/FPGA/AUDIO: track 85.6 -> 49.8 mm, vias 2 -> 0
- net Net-(J1-Pad4): track 26.0 -> 0.00 mm
- net /MAGIC/MCU/I2C0_SDA: track 50.0 -> 74.8 mm
- net /MAGIC/FPGA/L12: track 0.00 -> 20.9 mm, vias 0 -> 1
- net Net-(R61-Pad2): track 20.8 -> 0.00 mm
- net Net-(J8-Pad3): track 0.00 -> 19.6 mm, vias 0 -> 2
- net /MAGIC/FPGA/SPI0_SCK: track 99.6 -> 80.6 mm, vias 2 -> 3
- net /MAGIC/FPGA/L20: track 0.00 -> 18.1 mm, vias 0 -> 1
- net /MAGIC/FPGA/L13: track 0.00 -> 17.7 mm
- net /MAGIC/FPGA/P00: track 0.00 -> 17.3 mm
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- removed copper zone on B.Cu, net GND
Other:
- board text added: "1V2"
- board text added: "3V3"
- board text added: "AUDIO"
- board text added: "CB0"
- board text added: "CB1"
- board text added: "L12"
- board text added: "L13"
- board text added: "L20"
- board text added: "L21"
- board text added: "L46"
- board text added: "L53"
- board text added: "N04"
- board text added: "N06"
- board text added: "N09"
- board text added: "P00"
- board text added: "P04"
- board text added: "P06"
- board text added: "P09"
- board text added: "R75"
- board text added: "~{OE}"
- board text added: "~{WE}"
- board text removed: "+1V2"
- board text removed: "+3V3"
- board text removed: "AUD"
- board text removed: "BOOTSEL"
- board text removed: "L65"
- board text removed: "L67"
- board text removed: "L68"
- board text removed: "~{RD}"
- board text removed: "~{WR}"
